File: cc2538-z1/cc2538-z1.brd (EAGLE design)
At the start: 56.8 x 34.5 mm, 92 parts, among them Q2 DMG6602SVT, U1 CC2538, U2 CC1120_RHM_32, U3 TPD2E001IDRLRQ1, U4 CP2103, U5 BSS138PS, U6 BSS138PS, U7 BSS138PS, X1 FA-128, X2 32MHz, X3 32.768K

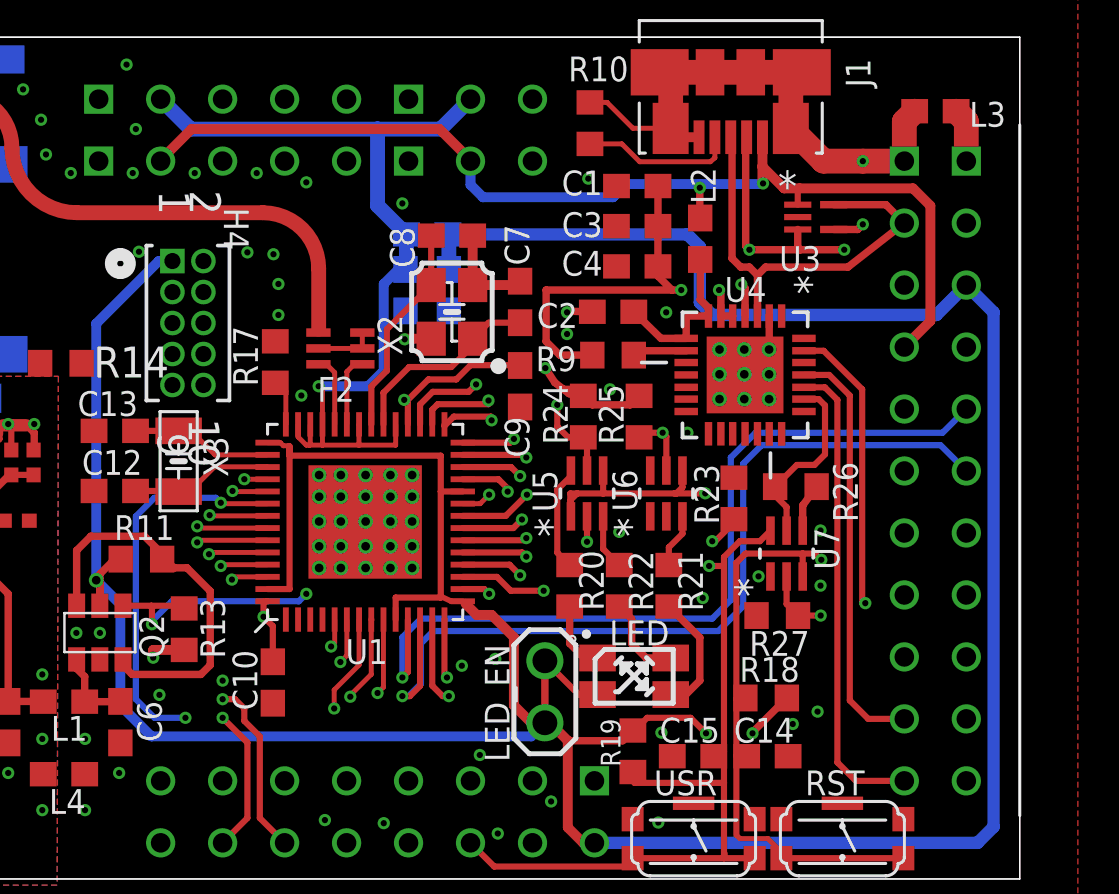
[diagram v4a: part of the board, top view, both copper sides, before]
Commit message: Added Serial > 3v3 diode.
Added I2C pullup

still need to work out SD SEL
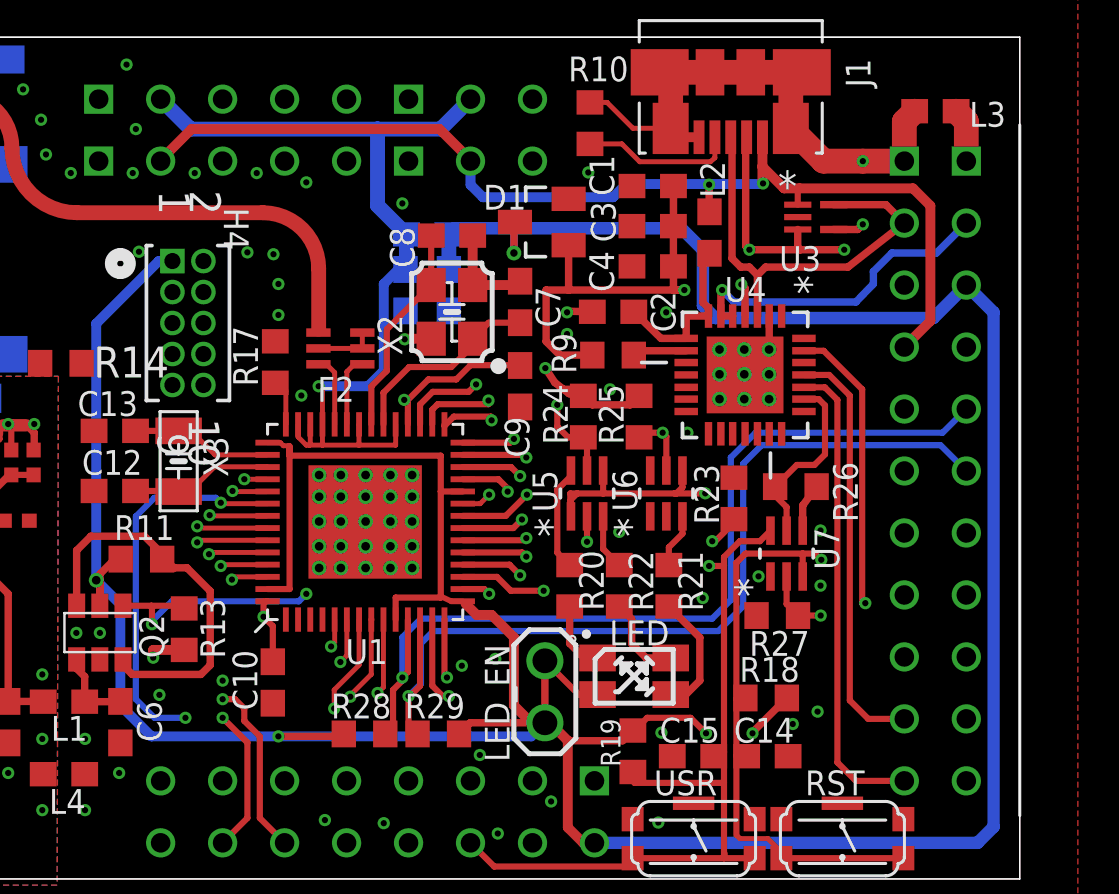
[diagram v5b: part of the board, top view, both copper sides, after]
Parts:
- added D1: BAT54S, diode:SOT23
- added R28, R29: 10k, rcl:R0603
- moved C3 0.64 mm to (41.8, 26.8)
- moved C1 0.63 mm to (41.8, 28.4)
- moved C4 0.63 mm to (41.8, 25.1)
- moved L2 0.46 mm to (44.1, 26.5)
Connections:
- net +3V3: now also D1.3, R28.2, R29.2
- net +3V3_SERIAL: now also D1.1
- net I2C_SCL: now also R28.1
- net I2C_SDA: now also R29.1
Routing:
- net +3V3: track 160.9 -> 170.1 mm, vias 5 -> 7
- net I2C_SCL: track 34.5 -> 37.4 mm
- net +3V3_SERIAL: track 29.8 -> 31.5 mm
- net I2C_SDA: track 35.8 -> 37.5 mm

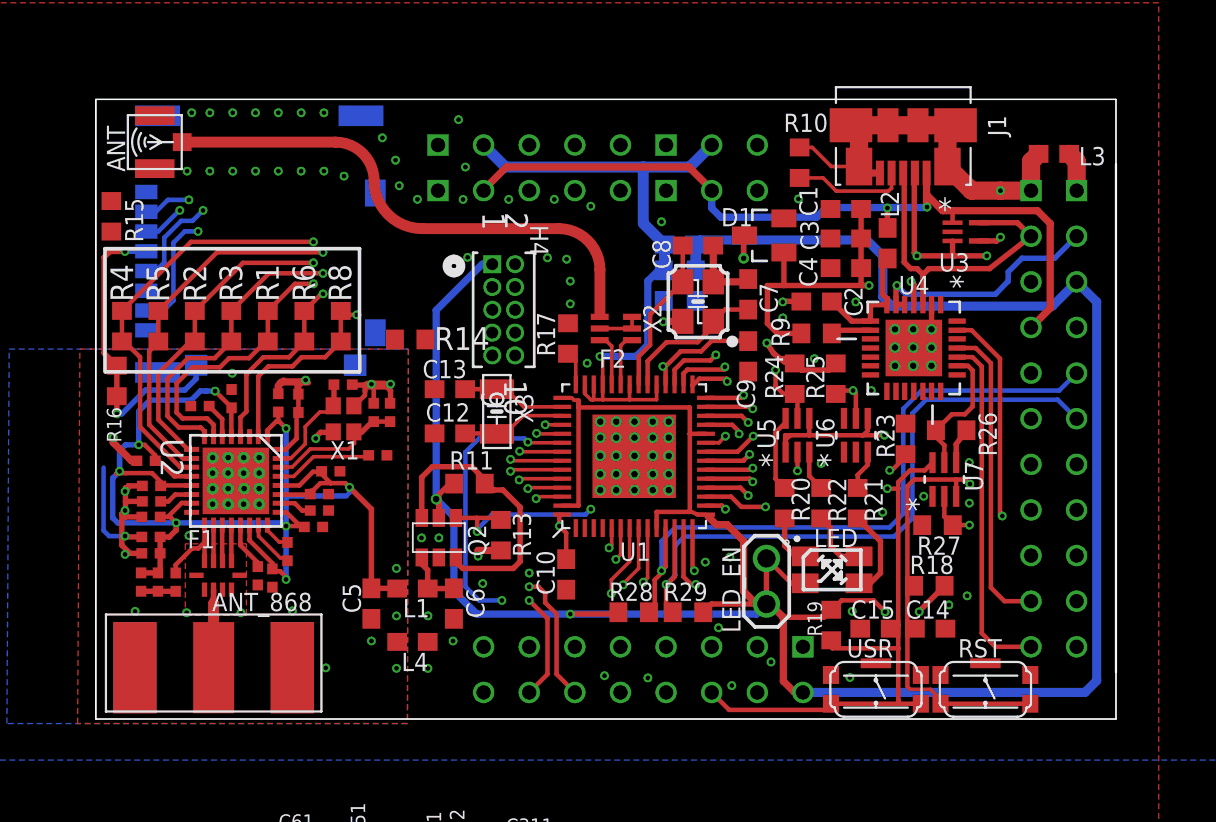
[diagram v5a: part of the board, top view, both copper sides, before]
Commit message: plit schematic into separate pages & added framesy
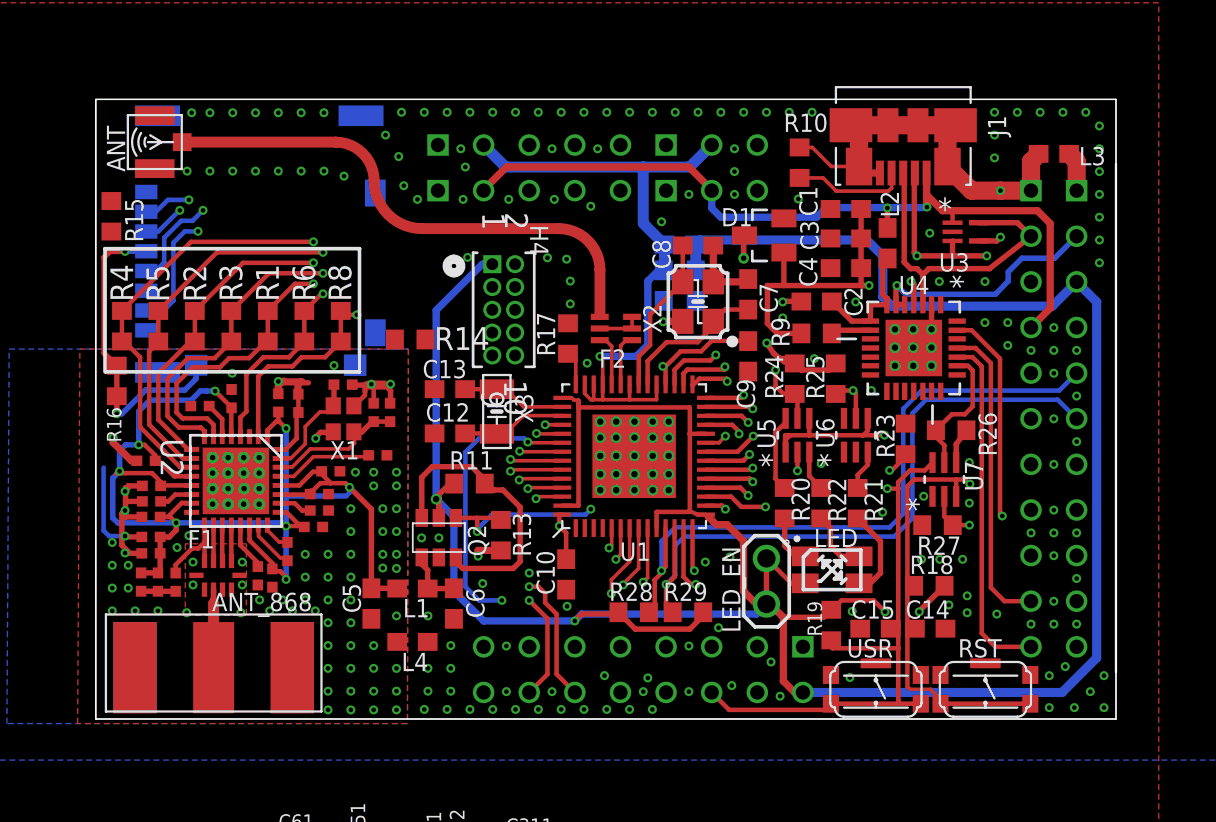
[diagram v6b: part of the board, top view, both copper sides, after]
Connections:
- net +5V: now also L2.1
- net +5V_USB: no longer L2.1
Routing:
- net +3V3: track 170.1 -> 171.4 mm
- net RGND: track 31.9 -> 31.6 mm, vias 20 -> 74
- net GND: vias 82 -> 180

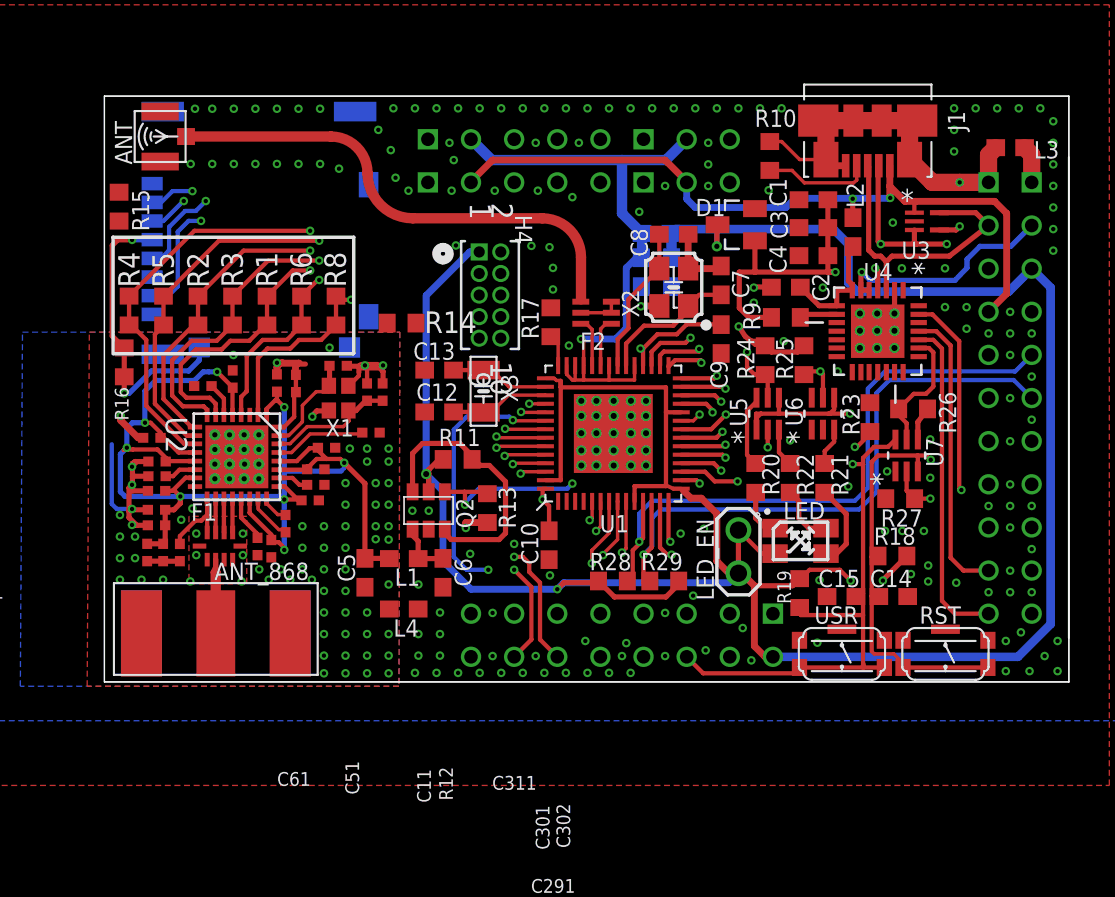
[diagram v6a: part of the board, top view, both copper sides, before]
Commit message: Added SPI Flash & moved 2.4G UFL
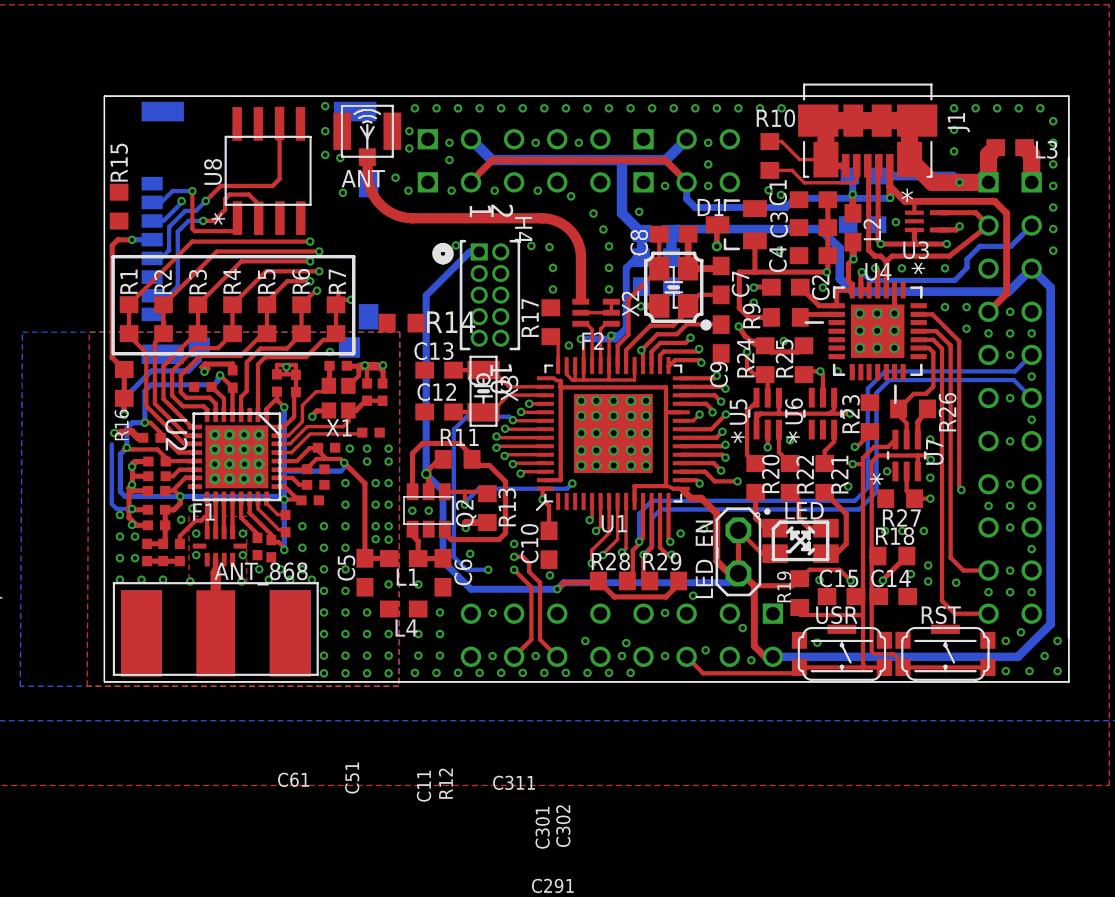
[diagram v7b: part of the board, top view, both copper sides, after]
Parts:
- removed R8: (no value), rcl:R0603
- added C18, C19: 100nf, CC11x:C0603
- added LED_EN: (no value), CC11x:1X02
- added R7: (no value), rcl:R0603
- added U8: M25P16VMN6P, CC11x:SOIC8
- moved ANT 12.2 mm to (15.5, 32.4), turned to 0 degrees
- moved R1 8.14 mm to (1.45, 21.4)
- moved R5 6.12 mm to (9.58, 21.4)
- moved R4 6.11 mm to (7.54, 21.4)
- moved R2 2.09 mm to (3.48, 21.4)
- moved R3 2.09 mm to (5.51, 21.4)
- moved R16 1.27 mm to (1.17, 17.6)
- moved R6 0.51 mm to (11.6, 21.4)
- moved L2 0.25 mm to (44.1, 26.7)
- moved C61 0.05 mm to (5.77, 17.4)
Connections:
- new net N$38: H1.A10
- net +3V3: now also LED_EN.1, LED_EN.2, U8.3, U8.8
- net +5V: now also C19.1; no longer L2.1
- net +5V_USB: now also C18.1, L2.1
- net GND: now also C19.2, U8.4
- net GNDA: now also C18.2
- net JTAG_TDI/DIO2: no longer H1.A10
- net RADIO_GPIO0: now also R2.1, R2.2; no longer R5.1, R5.2
- net RADIO_RESET_N: now also R7.1, R7.2; no longer R8.1, R8.2
- net RADIO_SPI_CLK: now also R4.1, R4.2; no longer R3.1, R3.2
- net RADIO_SPI_CSN: now also R1.1, R1.2; no longer R4.1, R4.2
- net RADIO_SPI_MISO: now also R3.1, R3.2; no longer R2.1, R2.2
- net RADIO_SPI_MOSI: now also R5.1, R5.2; no longer R1.1, R1.2
- net SD_SEL: now also U8.7
- net SD_SPI_CLK: now also U8.6
- net SD_SPI_CSN: now also U8.1
- net SD_SPI_MISO: now also U8.2
- net SD_SPI_MOSI: now also U8.5
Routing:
- net 2.4G: track 28.8 -> 18.2 mm
- net SD_SPI_CLK: track 53.4 -> 61.6 mm
- net SD_SPI_CSN: track 44.0 -> 49.6 mm
- net SD_SPI_MISO: track 55.9 -> 61.3 mm
- net GNDA: track 27.2 -> 32.1 mm
- net +5V: track 7.20 -> 9.67 mm, vias 0 -> 1
- net SD_SEL: track 58.4 -> 60.8 mm
- net +3V3_ANALOGUE: track 37.3 -> 39.6 mm, vias 1 -> 2
- net RGND: track 31.6 -> 33.8 mm
- net +5V_USB: track 45.0 -> 46.3 mm
- net RADIO_SPI_CSN: track 64.5 -> 63.4 mm
- net RADIO_SPI_CLK: track 73.4 -> 72.5 mm
- net RADIO_SPI_MISO: track 81.4 -> 80.5 mm
- net RADIO_SPI_MOSI: track 72.6 -> 71.8 mm
- net RADIO_GPIO2: track 54.4 -> 53.7 mm
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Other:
- board text removed: "LED_EN"

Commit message: Routing finished? need to sanity check.
Check pull ups for SPI
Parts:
- added R8: 56k, rcl:R0603
- added U10: DMG6602SVT, farnell-parts:TSOT26
- R14: value 100k -> 100K
- R15: value DNP -> 100K
- R16: value (none) -> DNP
- R17: value 56k -> DNP
- moved R17 21.0 mm to (5.74, 25.6), turned to 180 degrees
- moved R14 16.0 mm to (2.29, 26.1)
- moved R16 15.0 mm to (13.3, 26.4)
- moved R15 1.49 mm to (2.29, 28.4), turned to 0 degrees
- moved U8 0.25 mm to (9.40, 30.5)
- renumbered Q2 to U9
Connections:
- removed net JTAG_TDI/DIO2: H4.8, U1.49
- removed net JTAG_TDO/DIO1: H1.C51, H4.6, U1.48
- removed net SD_SEL: R14.1, R15.1, R16.1, R16.2, SD1.4, SD1.SWITCH, U1.22, U8.7
- new net JTAG_TDI/FLASH_SPI_CSN: H4.8, U1.49, U8.1
- new net JTAG_TDO/SD_PRESENCE: H4.6, R17.2, SD1.DETECT, U1.48
- new net MEM_VCC: R16.1, R16.2, R17.1, SD1.4, U10.P$4, U8.3, U8.7, U8.8
- new net N$41: H1.C51
- new net N$43: R15.1, U10.P$3, U10.P$6
- new net PWR_MEM_EN: R14.2, U1.22, U10.P$1
- net +3V3: now also U10.P$2; no longer SD1.DETECT, U8.3, U8.8
- net GND: now also R14.1, R8.2, SD1.SWITCH, U10.P$5; no longer R14.2, R17.2
- net N$21: now also R8.1; no longer R17.1
- net SD_SPI_CSN: no longer U8.1
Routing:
- net SD_SEL: track 60.8 -> 0.00 mm, vias 5 -> 0
- net JTAG_TDI/FLASH_SPI_CSN: track 0.00 -> 57.8 mm, vias 0 -> 3
- net PWR_MEM_EN: track 0.00 -> 54.0 mm, vias 0 -> 4
- net MEM_VCC: track 0.00 -> 49.3 mm, vias 0 -> 5
- net JTAG_TDO/SD_PRESENCE: track 0.00 -> 48.6 mm, vias 0 -> 3
- net JTAG_TDI/DIO2: track 28.3 -> 0.00 mm, vias 1 -> 0
- net JTAG_TDO/DIO1: track 27.9 -> 0.00 mm, vias 2 -> 0
- net +3V3: track 171.1 -> 195.7 mm, vias 5 -> 6
- net SD_SPI_MOSI: track 54.4 -> 63.1 mm, vias 3 -> 4
- net GND: track 81.5 -> 87.4 mm, vias 176 -> 182
- net N$43: track 0.00 -> 5.59 mm
- net SD_SPI_CSN: track 49.6 -> 44.0 mm
- net RGND: track 33.8 -> 36.1 mm, vias 74 -> 73
- net UART0_TX: track 64.1 -> 65.0 mm
- net RADIO_RESET_N: track 48.5 -> 47.8 mm
